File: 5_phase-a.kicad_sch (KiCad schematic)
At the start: 28 parts, among them Q501 BSC072N08NS5, Q502 BSC072N08NS5, U501 IR2181S, U502 AD8418

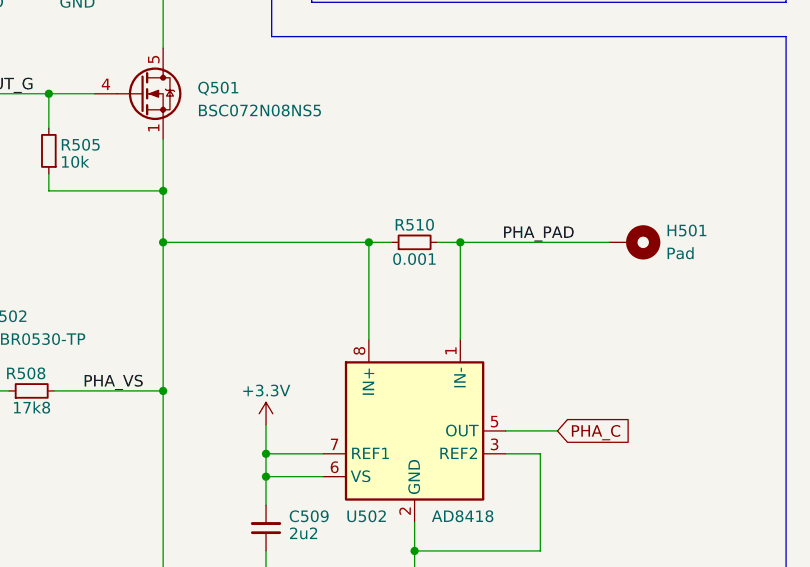
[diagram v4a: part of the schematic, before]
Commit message: feat: component placement for 1 phase completed
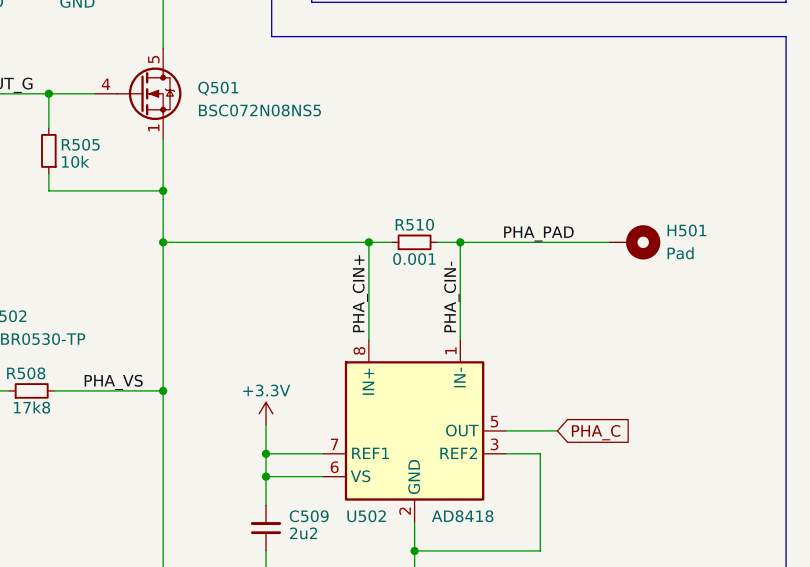
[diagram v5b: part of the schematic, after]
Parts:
- H501: footprint TestPoint:TestPoint_THTPad_4.0x4.0mm_Drill2.0mm -> TestPoint:TestPoint_Pad_5.0x7.0mm
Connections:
- net PHA_PAD renamed PHA_CIN-
- net PHA_VS renamed PHA_CIN+
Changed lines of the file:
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@@
     (effects (font (size 1.27 1.27)) (justify right bottom))
+  )
+  (label "PHA_CIN+" (at 232.41 93.345 90) (fields_autoplaced)
+    (effects (font (size 1.27 1.27)) (justify left bottom))
   )
   (label "PHA_IR_HIN" (at 68.58 90.805 0) (fields_autoplaced)
@@
   (label "PHA_VS" (at 106.68 95.885 180) (fields_autoplaced)
     (effects (font (size 1.27 1.27)) (justify right bottom))
+  )
+  (label "PHA_CIN-" (at 242.57 93.345 90) (fields_autoplaced)
+    (effects (font (size 1.27 1.27)) (justify left bottom))
   )
   (label "PHA_LOUT_G" (at 183.515 133.35 0) (fields_autoplaced)
@@
       (effects (font (size 1.27 1.27)) (justify left))
     )
-    (property "Footprint" "TestPoint:TestPoint_THTPad_4.0x4.0mm_Drill2.0mm" (at 261.62 83.185 0)
+    (property "Footprint" "TestPoint:TestPoint_Pad_5.0x7.0mm" (at 261.62 83.185 0)
       (effects (font (size 1.27 1.27)) hide)
     )

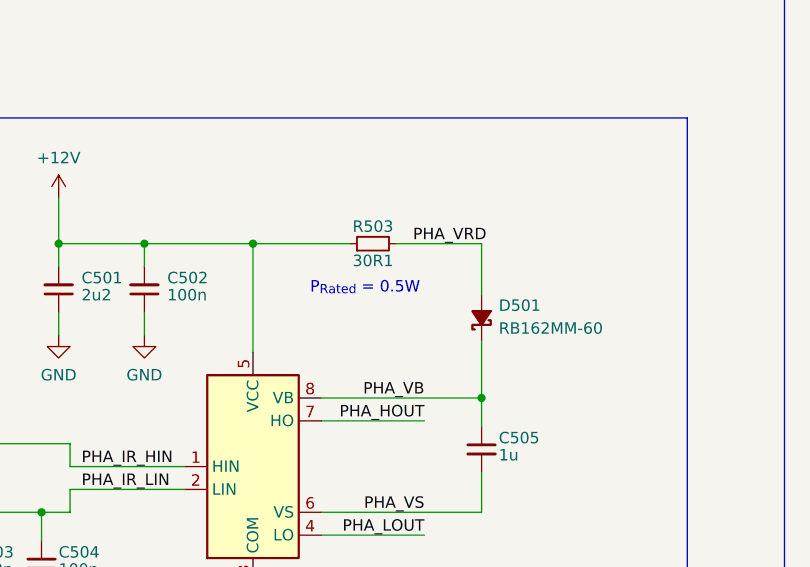
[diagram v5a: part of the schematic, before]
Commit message: fix: fixed LTSpice simulation and updated track widths accordingly
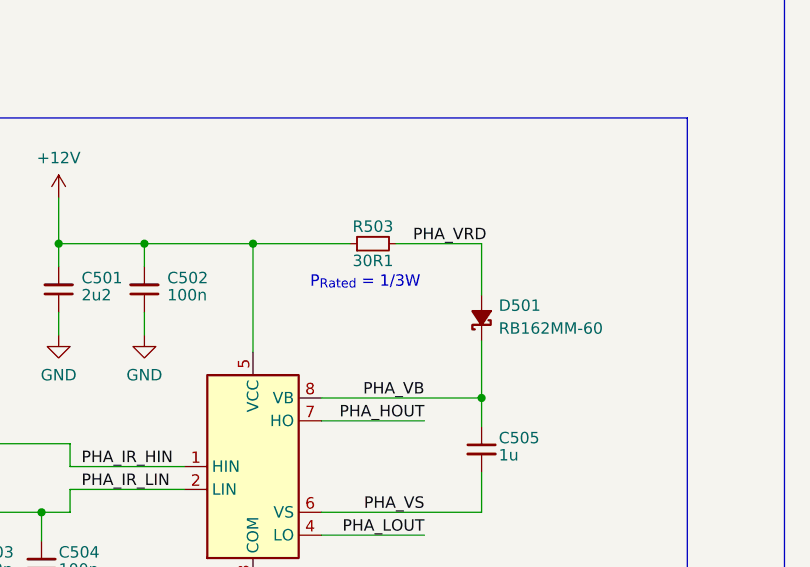
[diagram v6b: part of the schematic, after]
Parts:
- R503: Link (none) -> https://www.digikey.de/en/products/detail/vishay-dale/CRCW0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
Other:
- note added: "P_{Rated} = 1/3W"
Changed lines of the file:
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@@
     (effects (font (size 1.6 1.6) italic) (justify left bottom))
   )
-  (text "P_{Rated} = 0.5W\n" (at 93.98 71.755 0)
+  (text "P_{Rated} = 1/3W\n" (at 93.98 71.12 0)
     (effects (font (size 1.27 1.27)) (justify left bottom))
   )
@@
       (effects (font (size 1.27 1.27)) hide)
     )
+    (property "Link" "https://www.digikey.de/en/products/detail/vishay-dale/CRCW060333R0FKEAHP/2222237" (at 100.965 66.04 0)
+      (effects (font (size 1.27 1.27)) hide)
+    )

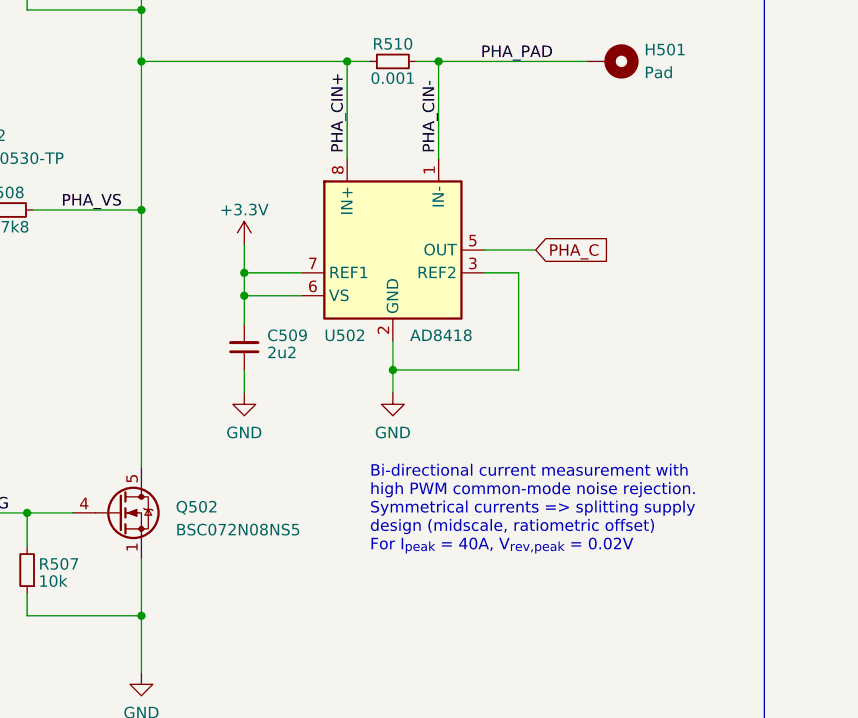
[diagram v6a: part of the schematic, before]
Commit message: feat: single phase, HSE, CAN routing and general layout
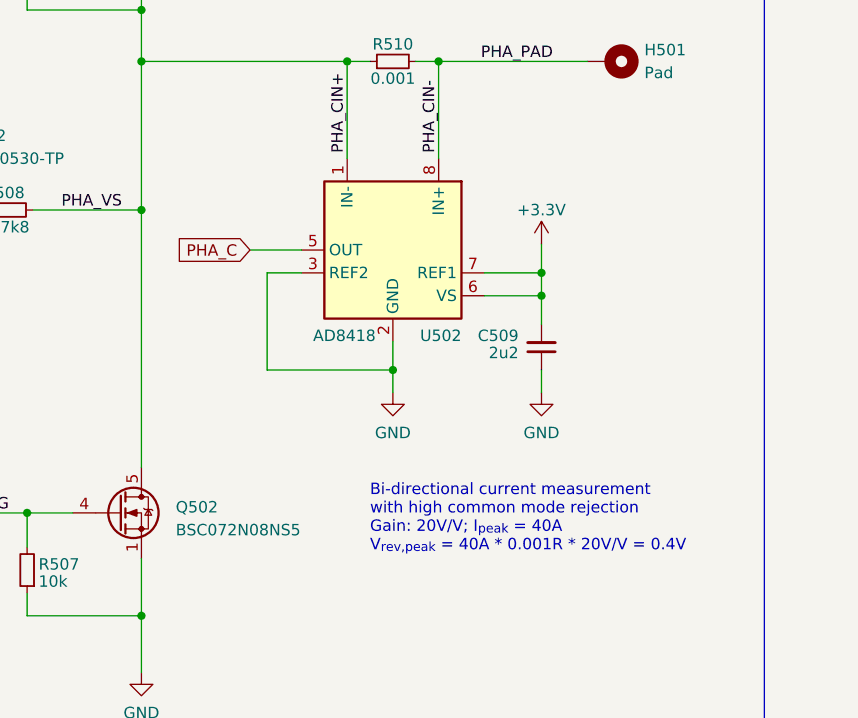
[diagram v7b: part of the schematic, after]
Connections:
- net PHA_CIN+: now also U502.1 (IN-); no longer U502.8 (IN+)
- net PHA_CIN-: now also U502.8 (IN+); no longer U502.1 (IN-)
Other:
- note added: "Bi-directional current measurement with high common mode rejection Gain: 20V/V; I_{peak} = 40A V_{rev,peak} = 40A * 0.001R * 20V/V = 0.4V"
- note removed: "Bi-directional current measurement with high PWM common-mode noise rejection. Symmetrical currents => splitting supply design (midscale, ratiometric offset) For I_{peak} = 40A, V_{rev,peak} = 0.02V"
- moved on the sheet: C509
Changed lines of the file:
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@@
   (junction (at 242.57 83.185) (diameter 0) (color 0 0 0 0)
   )
-  (junction (at 220.98 109.22) (diameter 0) (color 0 0 0 0)
+  (junction (at 254 109.22) (diameter 0) (color 0 0 0 0)
   )
   (junction (at 187.96 99.695) (diameter 0) (color 0 0 0 0)
@@
   (junction (at 173.99 109.855) (diameter 0) (color 0 0 0 0)
   )
-  (junction (at 220.98 106.68) (diameter 0) (color 0 0 0 0)
+  (junction (at 254 106.68) (diameter 0) (color 0 0 0 0)
   )
   (junction (at 75.565 66.04) (diameter 0) (color 0 0 0 0)
@@
     (stroke (width 0) (type default))
   )
-  (wire (pts (xy 220.98 109.22) (xy 220.98 106.68))
+  (wire (pts (xy 254 109.22) (xy 254 106.68))
     (stroke (width 0) (type default))
   )
@@
     (stroke (width 0) (type default))
   )
-  (wire (pts (xy 220.98 109.22) (xy 220.98 112.395))
+  (wire (pts (xy 254 109.22) (xy 254 112.395))
     (stroke (width 0) (type default))
   )
@@
     (stroke (width 0) (type default))
   )
-  (wire (pts (xy 247.65 106.68) (xy 251.46 106.68))
+  (wire (pts (xy 227.33 106.68) (xy 223.52 106.68))
     (stroke (width 0) (type default))
   )
@@
     (stroke (width 0) (type default))
   )
-  (wire (pts (xy 220.98 106.68) (xy 227.33 106.68))
+  (wire (pts (xy 254 106.68) (xy 247.65 106.68))
     (stroke (width 0) (type default))
   )
@@
     (stroke (width 0) (type default))
   )
-  (wire (pts (xy 247.65 104.14) (xy 253.365 104.14))
+  (wire (pts (xy 227.33 104.14) (xy 221.615 104.14))
     (stroke (width 0) (type default))
   )
@@
     (stroke (width 0) (type default))
   )
-  (wire (pts (xy 251.46 106.68) (xy 251.46 117.475))
+  (wire (pts (xy 223.52 106.68) (xy 223.52 117.475))
     (stroke (width 0) (type default))
   )
@@
     (stroke (width 0) (type default))
   )
-  (wire (pts (xy 220.98 117.475) (xy 220.98 120.015))
+  (wire (pts (xy 254 117.475) (xy 254 120.015))
     (stroke (width 0) (type default))
   )
@@
     (stroke (width 0) (type default))
   )
-  (wire (pts (xy 237.49 117.475) (xy 251.46 117.475))
+  (wire (pts (xy 237.49 117.475) (xy 223.52 117.475))
     (stroke (width 0) (type default))
   )
@@
     (stroke (width 0) (type default))
   )
-  (wire (pts (xy 227.33 109.22) (xy 220.98 109.22))
+  (wire (pts (xy 247.65 109.22) (xy 254 109.22))
     (stroke (width 0) (type default))
   )
@@
     (stroke (width 0) (type default))
   )
-  (wire (pts (xy 220.98 103.505) (xy 220.98 106.68))
+  (wire (pts (xy 254 103.505) (xy 254 106.68))
     (stroke (width 0) (type default))
   )
@@
     (effects (font (size 1.27 1.27)) (justify left bottom))
   )
-  (text "Bi-directional current measurement with\nhigh PWM common-mode noise rejection.\nSymmetrical currents => splitting supply\ndesign (midscale, ratiometric offset)\nFor I_{peak} = 40A, V_{rev,peak} = 0.02V"
+  (text "Bi-directional current measurement\nwith high common mode rejection\nGain: 20V/V; I_{peak} = 40A\nV_{rev,peak} = 40A * 0.001R * 20V/V = 0.4V"
     (at 234.95 137.795 0)
     (effects (font (size 1.27 1.27)) (justify left bottom))
@@
     )
   )
-  (global_label "PHA_C" (shape input) (at 253.365 104.14 0) (fields_autoplaced)
-    (effects (font (size 1.27 1.27)) (justify left))
-    (property "Intersheetrefs" "${INTERSHEET_REFS}" (at 261.7048 104.0606 0)
-      (effects (font (size 1.27 1.27)) (justify left) hide)
+  (global_label "PHA_C" (shape input) (at 221.615 104.14 180) (fields_autoplaced)
+    (effects (font (size 1.27 1.27)) (justify right))
+    (property "Intersheetrefs" "${INTERSHEET_REFS}" (at 213.2752 104.0606 0)
+      (effects (font (size 1.27 1.27)) (justify right) hide)
     )
   )
@@
     )
   )
-  (symbol (lib_id "power:GND") (at 220.98 120.015 0) (unit 1)
-    (in_bom yes) (on_board yes) (dnp no)
-    (property "Reference" "#PWR0144" (at 220.98 126.365 0)
-      (effects (font (size 1.27 1.27)) hide)
-    )
-    (property "Value" "GND" (at 220.98 124.46 0)
-      (effects (font (size 1.27 1.27)))
-    )
-    (property "Footprint" "" (at 220.98 120.015 0)
-      (effects (font (size 1.27 1.27)) hide)
-    )
-    (property "Datasheet" "" (at 220.98 120.015 0)
+  (symbol (lib_id "power:GND") (at 254 120.015 0) (mirror y) (unit 1)
+    (in_bom yes) (on_board yes) (dnp no)
+    (property "Reference" "#PWR0144" (at 254 126.365 0)
+      (effects (font (size 1.27 1.27)) hide)
+    )
+    (property "Value" "GND" (at 254 124.46 0)
+      (effects (font (size 1.27 1.27)))
+    )
+    (property "Footprint" "" (at 254 120.015 0)
+      (effects (font (size 1.27 1.27)) hide)
+    )
+    (property "Datasheet" "" (at 254 120.015 0)
       (effects (font (size 1.27 1.27)) hide)
     )
@@
     )
   )
-  (symbol (lib_id "power:+3.3V") (at 220.98 103.505 0) (unit 1)
-    (in_bom yes) (on_board yes) (dnp no)
-    (property "Reference" "#PWR0147" (at 220.98 107.315 0)
-      (effects (font (size 1.27 1.27)) hide)
-    )
-    (property "Value" "+3.3V" (at 220.98 99.695 0)
-      (effects (font (size 1.27 1.27)))
-    )
-    (property "Footprint" "" (at 220.98 103.505 0)
-      (effects (font (size 1.27 1.27)) hide)
-    )
-    (property "Datasheet" "" (at 220.98 103.505 0)
+  (symbol (lib_id "power:+3.3V") (at 254 103.505 0) (mirror y) (unit 1)
+    (in_bom yes) (on_board yes) (dnp no)
+    (property "Reference" "#PWR0147" (at 254 107.315 0)
+      (effects (font (size 1.27 1.27)) hide)
+    )
+    (property "Value" "+3.3V" (at 254 99.695 0)
+      (effects (font (size 1.27 1.27)))
+    )
+    (property "Footprint" "" (at 254 103.505 0)
+      (effects (font (size 1.27 1.27)) hide)
+    )
+    (property "Datasheet" "" (at 254 103.505 0)
       (effects (font (size 1.27 1.27)) hide)
     )
@@
     )
   )
-  (symbol (lib_id "Amplifier_Current:AD8418") (at 237.49 104.14 0) (unit 1)
-    (in_bom yes) (on_board yes) (dnp no)
-    (property "Reference" "U502" (at 229.87 113.665 0)
-      (effects (font (size 1.27 1.27)) (justify left))
-    )
-    (property "Value" "AD8418" (at 239.395 113.665 0)
-      (effects (font (size 1.27 1.27)) (justify left))
-    )
-    (property "Footprint" "Package_SO:SOIC-8_3.9x4.9mm_P1.27mm" (at 238.76 113.03 0)
-      (effects (font (size 1.27 1.27)) hide)
-    )
-    (property "Datasheet" "https://www.analog.com/media/en/technical-documentation/data-sheets/AD8418.pdf" (at 254 121.92 0)
+  (symbol (lib_id "Amplifier_Current:AD8418") (at 237.49 104.14 0) (mirror y) (unit 1)
+    (in_bom yes) (on_board yes) (dnp no)
+    (property "Reference" "U502" (at 245.11 113.665 0)
+      (effects (font (size 1.27 1.27)) (justify left))
+    )
+    (property "Value" "AD8418" (at 235.585 113.665 0)
+      (effects (font (size 1.27 1.27)) (justify left))
+    )
+    (property "Footprint" "Package_SO:SOIC-8_3.9x4.9mm_P1.27mm" (at 236.22 113.03 0)
+      (effects (font (size 1.27 1.27)) hide)
+    )
+    (property "Datasheet" "https://www.analog.com/media/en/technical-documentation/data-sheets/AD8418.pdf" (at 220.98 121.92 0)
       (effects (font (size 1.27 1.27)) hide)
     )
@@
     )
   )
-  (symbol (lib_id "Device:C_Small") (at 220.98 114.935 180) (unit 1)
-    (in_bom yes) (on_board yes) (dnp no)
-    (property "Reference" "C509" (at 223.52 113.665 0)
-      (effects (font (size 1.27 1.27)) (justify right))
-    )
-    (property "Value" "2u2" (at 223.52 115.57 0)
-      (effects (font (size 1.27 1.27)) (justify right))
-    )
-    (property "Footprint" "Capacitor_SMD:C_0603_1608Metric_Pad1.08x0.95mm_HandSolder" (at 220.98 114.935 0)
-      (effects (font (size 1.27 1.27)) hide)
-    )
-    (property "Datasheet" "~" (at 220.98 114.935 0)
+  (symbol (lib_id "Device:C_Small") (at 254 114.935 0) (mirror x) (unit 1)
+    (in_bom yes) (on_board yes) (dnp no)
+    (property "Reference" "C509" (at 251.46 113.665 0)
+      (effects (font (size 1.27 1.27)) (justify right))
+    )
+    (property "Value" "2u2" (at 251.46 115.57 0)
+      (effects (font (size 1.27 1.27)) (justify right))
+    )
+    (property "Footprint" "Capacitor_SMD:C_0603_1608Metric_Pad1.08x0.95mm_HandSolder" (at 254 114.935 0)
+      (effects (font (size 1.27 1.27)) hide)
+    )
+    (property "Datasheet" "~" (at 254 114.935 0)
       (effects (font (size 1.27 1.27)) hide)
     )
@@
     )
   )
-  (symbol (lib_id "power:GND") (at 237.49 120.015 0) (unit 1)
+  (symbol (lib_id "power:GND") (at 237.49 120.015 0) (mirror y) (unit 1)
     (in_bom yes) (on_board yes) (dnp no)
     (property "Reference" "#PWR0143" (at 237.49 126.365 0)
